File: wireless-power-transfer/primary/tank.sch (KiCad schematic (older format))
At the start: 6 parts

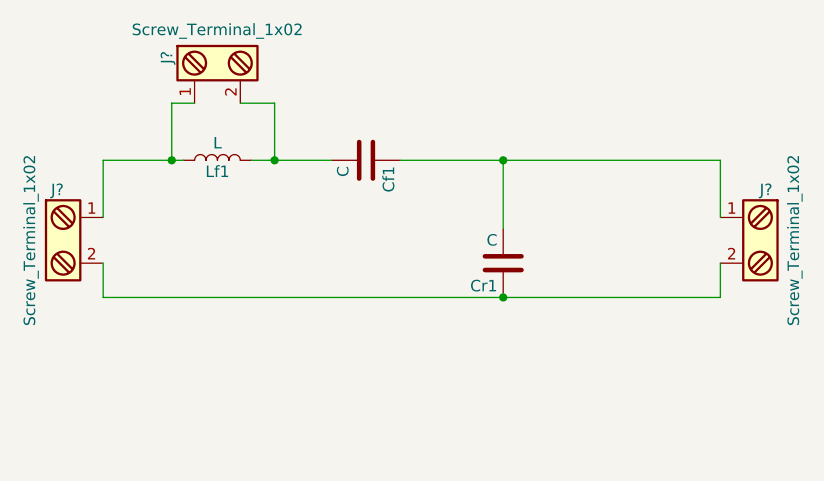
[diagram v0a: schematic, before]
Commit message: Added pcb with tank and filter of the primary, some logos and other minor changes.
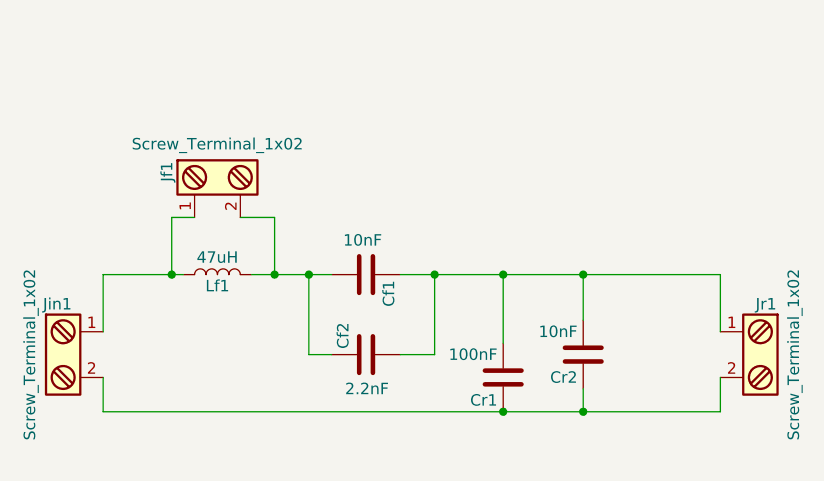
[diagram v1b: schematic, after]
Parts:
- added Cf2: 2.2nF, Capacitors_THT:C_Rect_L18.0mm_W5.0mm_P15.00mm_FKS3_FKP3, symbol C
- added Cr2: 10nF, Capacitors_THT:C_Rect_L18.0mm_W6.0mm_P15.00mm_FKS3_FKP3, symbol C
- Cf1: value C -> 10nF; footprint (none) -> Capacitors_THT:C_Rect_L18.0mm_W6.0mm_P15.00mm_FKS3_FKP3
- Cr1: value C -> 100nF; footprint (none) -> Capacitors_THT:C_Rect_L18.0mm_W5.0mm_P15.00mm_FKS3_FKP3
- Jf1, Jin1, Jr1: renamed from J?; footprint (none) -> Connectors_Terminal_Blocks:TerminalBlock_Pheonix_MKDS1.5-2pol
- Lf1: value L -> 47uH; footprint (none) -> componentesGIT:MuRata 1500 47u
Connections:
- net at Cr1.1, Jin1.2, Jr1.2: now also Cr2.1
- net at Cf1.2, Jf1.2, Lf1.2: now also Cf2.1
- net at Cf1.1, Cr1.2, Jr1.1: now also Cf2.2, Cr2.2
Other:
- moved on the sheet: Cf1, Cr1, Jf1, Jin1, Jr1, Lf1
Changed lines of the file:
@@
 $EndDescr
 $Comp
-L Screw_Terminal_1x02 J?
+L Screw_Terminal_1x02 Jin1
 U 1 1 59F1ACFF
-P 4500 3150
-F 0 "J?" H 4500 3400 50  0000 C TNN
-F 1 "Screw_Terminal_1x02" V 4350 3150 50  0000 C TNN
-F 2 "" H 4500 2925 50  0001 C CNN
-F 3 "" H 4475 3150 50  0001 C CNN
-	1    4500 3150
+P 4500 3650
+F 0 "Jin1" H 4500 3900 50  0000 C TNN
+F 1 "Screw_Terminal_1x02" V 4350 3650 50  0000 C TNN
+F 2 "Connectors_Terminal_Blocks:TerminalBlock_Pheonix_MKDS1.5-2pol" H 4500 3425 50  0001 C CNN
+F 3 "" H 4475 3650 50  0001 C CNN
+	1    4500 3650
 	1    0    0    -1
 $EndComp
@@
 L L Lf1
 U 1 1 59F1AF47
-P 5200 2800
-F 0 "Lf1" V 5150 2800 50  0000 C CNN
-F 1 "L" V 5275 2800 50  0000 C CNN
-F 2 "" H 5200 2800 50  0001 C CNN
-F 3 "" H 5200 2800 50  0001 C CNN
-	1    5200 2800
+P 5200 3300
+F 0 "Lf1" V 5150 3300 50  0000 C CNN
+F 1 "47uH" V 5275 3300 50  0000 C CNN
+F 2 "componentesGIT:MuRata 1500 47u" H 5200 3300 50  0001 C CNN
+F 3 "" H 5200 3300 50  0001 C CNN
+	1    5200 3300
 	0    -1   -1   0
 $EndComp
@@
 L C Cf1
 U 1 1 59F1B01C
-P 5850 2800
-F 0 "Cf1" H 5875 2900 50  0000 L CNN
-F 1 "C" H 5875 2700 50  0000 L CNN
-F 2 "" H 5888 2650 50  0001 C CNN
-F 3 "" H 5850 2800 50  0001 C CNN
-	1    5850 2800
+P 5850 3300
+F 0 "Cf1" H 5875 3400 50  0000 L CNN
+F 1 "10nF" V 5700 3200 50  0000 L CNN
+F 2 "Capacitors_THT:C_Rect_L18.0mm_W6.0mm_P15.00mm_FKS3_FKP3" H 5888 3150 50  0001 C CNN
+F 3 "" H 5850 3300 50  0001 C CNN
+	1    5850 3300
 	0    1    1    0
 $EndComp
@@
 L C Cr1
 U 1 1 59F1B0F0
-P 6450 3250
-F 0 "Cr1" H 6475 3350 50  0000 L CNN
-F 1 "C" H 6475 3150 50  0000 L CNN
-F 2 "" H 6488 3100 50  0001 C CNN
-F 3 "" H 6450 3250 50  0001 C CNN
-	1    6450 3250
+P 6450 3750
+F 0 "Cr1" H 6475 3850 50  0000 L CNN
+F 1 "100nF" H 6475 3650 50  0000 L CNN
+F 2 "Capacitors_THT:C_Rect_L18.0mm_W5.0mm_P15.00mm_FKS3_FKP3" H 6488 3600 50  0001 C CNN
+F 3 "" H 6450 3750 50  0001 C CNN
+	1    6450 3750
 	-1   0    0    1
 $EndComp
 $Comp
-L Screw_Terminal_1x02 J?
+L Screw_Terminal_1x02 Jr1
 U 1 1 59F1B13E
-P 7600 3150
-F 0 "J?" H 7600 3400 50  0000 C TNN
-F 1 "Screw_Terminal_1x02" V 7450 3150 50  0000 C TNN
-F 2 "" H 7600 2925 50  0001 C CNN
-F 3 "" H 7575 3150 50  0001 C CNN
-	1    7600 3150
+P 7600 3650
+F 0 "Jr1" H 7600 3900 50  0000 C TNN
+F 1 "Screw_Terminal_1x02" V 7450 3650 50  0000 C TNN
+F 2 "Connectors_Terminal_Blocks:TerminalBlock_Pheonix_MKDS1.5-2pol" H 7600 3425 50  0001 C CNN
+F 3 "" H 7575 3650 50  0001 C CNN
+	1    7600 3650
 	-1   0    0    -1
 $EndComp
 Wire Wire Line
-	4700 3050 4700 2800
+	4700 3550 4700 3300
 Wire Wire Line
-	4700 2800 5050 2800
+	4700 3300 5050 3300
 Wire Wire Line
-	5350 2800 5700 2800
+	5350 3300 5700 3300
 Wire Wire Line
-	6000 2800 7400 2800
+	6000 3300 7400 3300
 Wire Wire Line
-	6450 2800 6450 3100
+	6450 3300 6450 3600
 Wire Wire Line
-	7400 2800 7400 3050
+	7400 3300 7400 3550
 Wire Wire Line
-	7400 3400 7400 3250
+	7400 3900 7400 3750
 Wire Wire Line
-	4700 3400 7400 3400
-Connection ~ 6450 2800
+	4700 3900 7400 3900
+Connection ~ 6450 3300
 Wire Wire Line
-	4700 3400 4700 3250
-Connection ~ 6450 3400
+	4700 3900 4700 3750
+Connection ~ 6450 3900
 $Comp
-L Screw_Terminal_1x02 J?
+L Screw_Terminal_1x02 Jf1
 U 1 1 59F1B5CA
-P 5200 2350
-F 0 "J?" H 5200 2600 50  0000 C TNN
-F 1 "Screw_Terminal_1x02" V 5050 2350 50  0000 C TNN
-F 2 "" H 5200 2125 50  0001 C CNN
-F 3 "" H 5175 2350 50  0001 C CNN
-	1    5200 2350
+P 5200 2850
+F 0 "Jf1" H 5200 3100 50  0000 C TNN
+F 1 "Screw_Terminal_1x02" V 5050 2850 50  0000 C TNN
+F 2 "Connectors_Terminal_Blocks:TerminalBlock_Pheonix_MKDS1.5-2pol" H 5200 2625 50  0001 C CNN
+F 3 "" H 5175 2850 50  0001 C CNN
+	1    5200 2850
 	0    -1   1    0
 $EndComp
 Wire Wire Line
-	5000 2800 5000 2550
+	5000 3300 5000 3050
 Wire Wire Line
-	5000 2550 5100 2550
-Connection ~ 5000 2800
+	5000 3050 5100 3050
+Connection ~ 5000 3300
 Wire Wire Line
-	5450 2800 5450 2550
+	5450 3300 5450 3050
 Wire Wire Line
-	5450 2550 5300 2550
-Connection ~ 5450 2800
+	5450 3050 5300 3050
+Connection ~ 5450 3300
+$Comp
+L C Cr2
+U 1 1 59F1A45D
+P 6800 3650
+F 0 "Cr2" H 6825 3750 50  0000 L CNN
+F 1 "10nF" H 6825 3550 50  0000 L CNN
+F 2 "Capacitors_THT:C_Rect_L18.0mm_W6.0mm_P15.00mm_FKS3_FKP3" H 6838 3500 50  0001 C CNN
+F 3 "" H 6800 3650 50  0001 C CNN
+	1    6800 3650
+	-1   0    0    1
+$EndComp
+$Comp
+L C Cf2
+U 1 1 59F1A4A3
+P 5850 3650
+F 0 "Cf2" H 5875 3750 50  0000 L CNN
+F 1 "2.2nF" V 5700 3550 50  0000 L CNN
+F 2 "Capacitors_THT:C_Rect_L18.0mm_W5.0mm_P15.00mm_FKS3_FKP3" H 5888 3500 50  0001 C CNN
+F 3 "" H 5850 3650 50  0001 C CNN
+	1    5850 3650
+	0    -1   -1   0
+$EndComp
+Wire Wire Line
+	6800 3500 6800 3300
+Connection ~ 6800 3300
+Wire Wire Line
+	6800 3800 6800 3900
+Connection ~ 6800 3900
+Wire Wire Line
+	6000 3650 6150 3650
+Wire Wire Line
+	6150 3650 6150 3300
+Connection ~ 6150 3300
+Wire Wire Line
+	5700 3650 5600 3650
+Wire Wire Line
+	5600 3650 5600 3300
+Connection ~ 5600 3300
 $EndSCHEMATC

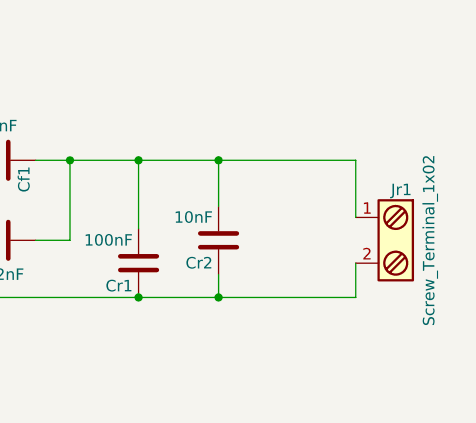
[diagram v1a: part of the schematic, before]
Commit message: Added a second connector for resonant coil of the primary.
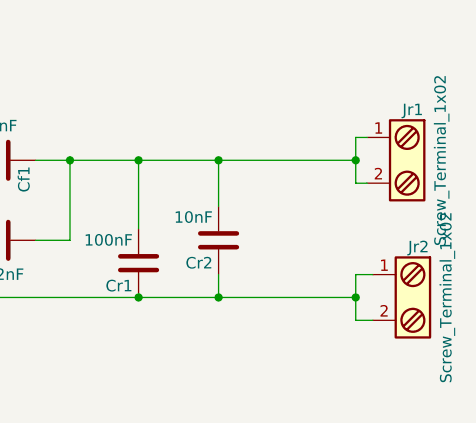
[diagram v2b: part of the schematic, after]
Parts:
- added Jr2: Screw_Terminal_1x02, Connectors_Terminal_Blocks:TerminalBlock_Pheonix_MKDS1.5-2pol, symbol Screw_Terminal_1x02
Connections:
- net at Cr1.1, Cr2.1, Jin1.2: now also Jr2.1, Jr2.2; no longer Jr1.2
- net at Cf1.1, Cf2.2, Cr1.2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: now also Jr1.2
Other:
- moved on the sheet: Jr1
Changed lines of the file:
@@
 L Screw_Terminal_1x02 Jr1
 U 1 1 59F1B13E
-P 7600 3650
-F 0 "Jr1" H 7600 3900 50  0000 C TNN
-F 1 "Screw_Terminal_1x02" V 7450 3650 50  0000 C TNN
-F 2 "Connectors_Terminal_Blocks:TerminalBlock_Pheonix_MKDS1.5-2pol" H 7600 3425 50  0001 C CNN
-F 3 "" H 7575 3650 50  0001 C CNN
-	1    7600 3650
+P 7650 3300
+F 0 "Jr1" H 7650 3550 50  0000 C TNN
+F 1 "Screw_Terminal_1x02" V 7500 3300 50  0000 C TNN
+F 2 "Connectors_Terminal_Blocks:TerminalBlock_Pheonix_MKDS1.5-2pol" H 7650 3075 50  0001 C CNN
+F 3 "" H 7625 3300 50  0001 C CNN
+	1    7650 3300
 	-1   0    0    -1
 $EndComp
@@
 Wire Wire Line
 	6450 3300 6450 3600
-Wire Wire Line
-	7400 3300 7400 3550
-Wire Wire Line
-	7400 3900 7400 3750
 Wire Wire Line
 	4700 3900 7400 3900
@@
 	5600 3650 5600 3300
 Connection ~ 5600 3300
+Wire Wire Line
+	7400 3200 7400 3400
+Wire Wire Line
+	7400 3200 7450 3200
+Wire Wire Line
+	7400 3400 7450 3400
+Connection ~ 7400 3300
+$Comp
+L Screw_Terminal_1x02 Jr2
+U 1 1 59F74076
+P 7675 3900
+F 0 "Jr2" H 7675 4150 50  0000 C TNN
+F 1 "Screw_Terminal_1x02" V 7525 3900 50  0000 C TNN
+F 2 "Connectors_Terminal_Blocks:TerminalBlock_Pheonix_MKDS1.5-2pol" H 7675 3675 50  0001 C CNN
+F 3 "" H 7650 3900 50  0001 C CNN
+	1    7675 3900
+	-1   0    0    -1
+$EndComp
+Wire Wire Line
+	7400 3800 7400 4000
+Wire Wire Line
+	7400 3800 7475 3800
+Wire Wire Line
+	7400 4000 7475 4000
+Connection ~ 7400 3900
 $EndSCHEMATC

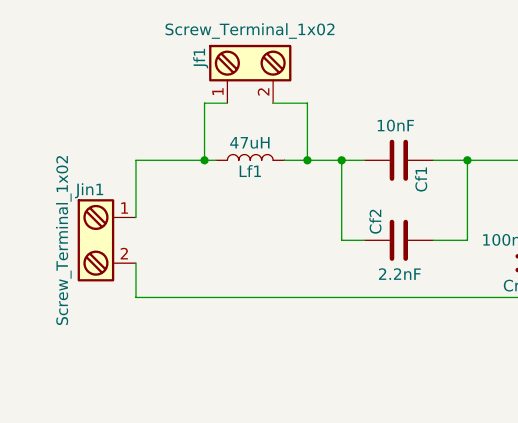
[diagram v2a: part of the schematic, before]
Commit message: The two PCBs of the primary circuit have been connected.
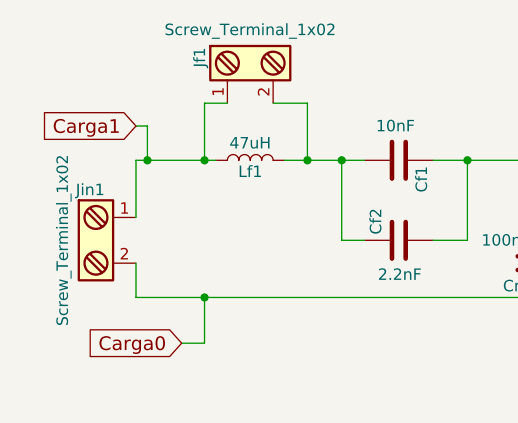
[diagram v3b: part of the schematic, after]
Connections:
- net Carga0: now reaches Cr1.1, Cr2.1, Jin1.2, Jr2.1, Jr2.2
- net Carga1: now reaches Jf1.1, Jin1.1, Lf1.1
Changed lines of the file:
@@
 LIBS:r-78exx
 LIBS:switches
-LIBS:xbee_wi-fi
 LIBS:irlb8721pbf
 LIBS:tfg-cache
@@
 	7400 4000 7475 4000
 Connection ~ 7400 3900
+Text GLabel 4700 3150 0    60   Input ~ 0
+Carga1
+Text GLabel 4900 4100 0    60   Input ~ 0
+Carga0
+Wire Wire Line
+	4700 3150 4750 3150
+Wire Wire Line
+	4750 3150 4750 3300
+Connection ~ 4750 3300
+Wire Wire Line
+	4900 4100 5000 4100
+Wire Wire Line
+	5000 4100 5000 3900
+Connection ~ 5000 3900
 $EndSCHEMATC

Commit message: PDFs created with schematics and PCB layers for front and back sides.
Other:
- note added: "2/7"
- moved on the sheet: Cf1, Cf2, Cr1, Cr2, Jf1, Jin1, Jr1, Jr2, Lf1
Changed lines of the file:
@@
 EESchema Schematic File Version 2
+LIBS:tfg-rescue
 LIBS:power
 LIBS:device
@@
 LIBS:r-78exx
 LIBS:switches
+LIBS:xbee_wi-fi
 LIBS:irlb8721pbf
 LIBS:tfg-cache
 EELAYER 25 0
 EELAYER END
-$Descr A4 11693 8268
+$Descr A4 8268 11693 portrait
 encoding utf-8
 Sheet 2 2
@@
 L Screw_Terminal_1x02 Jin1
 U 1 1 59F1ACFF
-P 4500 3650
-F 0 "Jin1" H 4500 3900 50  0000 C TNN
-F 1 "Screw_Terminal_1x02" V 4350 3650 50  0000 C TNN
-F 2 "Connectors_Terminal_Blocks:TerminalBlock_Pheonix_MKDS1.5-2pol" H 4500 3425 50  0001 C CNN
-F 3 "" H 4475 3650 50  0001 C CNN
-	1    4500 3650
+P 2800 4500
+F 0 "Jin1" H 2800 4750 50  0000 C TNN
+F 1 "Screw_Terminal_1x02" V 2650 4500 50  0000 C TNN
+F 2 "Connectors_Terminal_Blocks:TerminalBlock_Pheonix_MKDS1.5-2pol" H 2800 4275 50  0001 C CNN
+F 3 "" H 2775 4500 50  0001 C CNN
+	1    2800 4500
 	1    0    0    -1
 $EndComp
@@
 L L Lf1
 U 1 1 59F1AF47
-P 5200 3300
-F 0 "Lf1" V 5150 3300 50  0000 C CNN
-F 1 "47uH" V 5275 3300 50  0000 C CNN
-F 2 "componentesGIT:MuRata 1500 47u" H 5200 3300 50  0001 C CNN
-F 3 "" H 5200 3300 50  0001 C CNN
-	1    5200 3300
+P 3500 4150
+F 0 "Lf1" V 3450 4150 50  0000 C CNN
+F 1 "47uH" V 3575 4150 50  0000 C CNN
+F 2 "componentesGIT:MuRata 1500 47u" H 3500 4150 50  0001 C CNN
+F 3 "" H 3500 4150 50  0001 C CNN
+	1    3500 4150
 	0    -1   -1   0
 $EndComp
@@
 L C Cf1
 U 1 1 59F1B01C
-P 5850 3300
-F 0 "Cf1" H 5875 3400 50  0000 L CNN
-F 1 "10nF" V 5700 3200 50  0000 L CNN
-F 2 "Capacitors_THT:C_Rect_L18.0mm_W6.0mm_P15.00mm_FKS3_FKP3" H 5888 3150 50  0001 C CNN
-F 3 "" H 5850 3300 50  0001 C CNN
-	1    5850 3300
+P 4150 4150
+F 0 "Cf1" V 4225 4200 50  0000 L CNN
+F 1 "10nF" V 4000 4050 50  0000 L CNN
+F 2 "Capacitors_THT:C_Rect_L18.0mm_W6.0mm_P15.00mm_FKS3_FKP3" H 4188 4000 50  0001 C CNN
+F 3 "" H 4150 4150 50  0001 C CNN
+	1    4150 4150
 	0    1    1    0
 $EndComp
@@
 L C Cr1
 U 1 1 59F1B0F0
-P 6450 3750
-F 0 "Cr1" H 6475 3850 50  0000 L CNN
-F 1 "100nF" H 6475 3650 50  0000 L CNN
-F 2 "Capacitors_THT:C_Rect_L18.0mm_W5.0mm_P15.00mm_FKS3_FKP3" H 6488 3600 50  0001 C CNN
-F 3 "" H 6450 3750 50  0001 C CNN
-	1    6450 3750
+P 4750 4450
+F 0 "Cr1" H 4775 4550 50  0000 L CNN
+F 1 "100nF" H 4775 4350 50  0000 L CNN
+F 2 "Capacitors_THT:C_Rect_L18.0mm_W5.0mm_P15.00mm_FKS3_FKP3" H 4788 4300 50  0001 C CNN
+F 3 "" H 4750 4450 50  0001 C CNN
+	1    4750 4450
 	-1   0    0    1
 $EndComp
@@
 L Screw_Terminal_1x02 Jr1
 U 1 1 59F1B13E
-P 7650 3300
-F 0 "Jr1" H 7650 3550 50  0000 C TNN
-F 1 "Screw_Terminal_1x02" V 7500 3300 50  0000 C TNN
-F 2 "Connectors_Terminal_Blocks:TerminalBlock_Pheonix_MKDS1.5-2pol" H 7650 3075 50  0001 C CNN
-F 3 "" H 7625 3300 50  0001 C CNN
-	1    7650 3300
+P 5950 4150
+F 0 "Jr1" H 5950 4400 50  0000 C TNN
+F 1 "Screw_Terminal_1x02" V 5800 4150 50  0000 C TNN
+F 2 "Connectors_Terminal_Blocks:TerminalBlock_Pheonix_MKDS1.5-2pol" H 5950 3925 50  0001 C CNN
+F 3 "" H 5925 4150 50  0001 C CNN
+	1    5950 4150
 	-1   0    0    -1
 $EndComp
 Wire Wire Line
-	4700 3550 4700 3300
-Wire Wire Line
-	4700 3300 5050 3300
-Wire Wire Line
-	5350 3300 5700 3300
-Wire Wire Line
-	6000 3300 7400 3300
-Wire Wire Line
-	6450 3300 6450 3600
-Wire Wire Line
-	4700 3900 7400 3900
-Connection ~ 6450 3300
-Wire Wire Line
-	4700 3900 4700 3750
-Connection ~ 6450 3900
+	3000 4400 3000 4150
+Wire Wire Line
+	3000 4150 3350 4150
+Wire Wire Line
+	3650 4150 4000 4150
+Wire Wire Line
+	4300 4150 5700 4150
+Wire Wire Line
+	3000 4750 5700 4750
+Connection ~ 4750 4150
+Wire Wire Line
+	3000 4750 3000 4600
+Connection ~ 4750 4750
 $Comp
 L Screw_Terminal_1x02 Jf1
 U 1 1 59F1B5CA
-P 5200 2850
-F 0 "Jf1" H 5200 3100 50  0000 C TNN
-F 1 "Screw_Terminal_1x02" V 5050 2850 50  0000 C TNN
-F 2 "Connectors_Terminal_Blocks:TerminalBlock_Pheonix_MKDS1.5-2pol" H 5200 2625 50  0001 C CNN
-F 3 "" H 5175 2850 50  0001 C CNN
-	1    5200 2850
+P 3500 3700
+F 0 "Jf1" H 3500 3950 50  0000 C TNN
+F 1 "Screw_Terminal_1x02" V 3350 3700 50  0000 C TNN
+F 2 "Connectors_Terminal_Blocks:TerminalBlock_Pheonix_MKDS1.5-2pol" H 3500 3475 50  0001 C CNN
+F 3 "" H 3475 3700 50  0001 C CNN
+	1    3500 3700
 	0    -1   1    0
 $EndComp
 Wire Wire Line
-	5000 3300 5000 3050
-Wire Wire Line
-	5000 3050 5100 3050
-Connection ~ 5000 3300
-Wire Wire Line
-	5450 3300 5450 3050
-Wire Wire Line
-	5450 3050 5300 3050
-Connection ~ 5450 3300
+	3300 4150 3300 3900
+Wire Wire Line
+	3300 3900 3400 3900
+Connection ~ 3300 4150
+Wire Wire Line
+	3750 4150 3750 3900
+Wire Wire Line
+	3750 3900 3600 3900
+Connection ~ 3750 4150
 $Comp
 L C Cr2
 U 1 1 59F1A45D
-P 6800 3650
-F 0 "Cr2" H 6825 3750 50  0000 L CNN
-F 1 "10nF" H 6825 3550 50  0000 L CNN
-F 2 "Capacitors_THT:C_Rect_L18.0mm_W6.0mm_P15.00mm_FKS3_FKP3" H 6838 3500 50  0001 C CNN
-F 3 "" H 6800 3650 50  0001 C CNN
-	1    6800 3650
+P 5100 4450
+F 0 "Cr2" H 5125 4550 50  0000 L CNN
+F 1 "10nF" H 5125 4350 50  0000 L CNN
+F 2 "Capacitors_THT:C_Rect_L18.0mm_W6.0mm_P15.00mm_FKS3_FKP3" H 5138 4300 50  0001 C CNN
+F 3 "" H 5100 4450 50  0001 C CNN
+	1    5100 4450
 	-1   0    0    1
 $EndComp
@@
 L C Cf2
 U 1 1 59F1A4A3
-P 5850 3650
-F 0 "Cf2" H 5875 3750 50  0000 L CNN
-F 1 "2.2nF" V 5700 3550 50  0000 L CNN
-F 2 "Capacitors_THT:C_Rect_L18.0mm_W5.0mm_P15.00mm_FKS3_FKP3" H 5888 3500 50  0001 C CNN
-F 3 "" H 5850 3650 50  0001 C CNN
-	1    5850 3650
+P 4150 4500
+F 0 "Cf2" V 4225 4325 50  0000 L CNN
+F 1 "2.2nF" V 4000 4400 50  0000 L CNN
+F 2 "Capacitors_THT:C_Rect_L18.0mm_W5.0mm_P15.00mm_FKS3_FKP3" H 4188 4350 50  0001 C CNN
+F 3 "" H 4150 4500 50  0001 C CNN
+	1    4150 4500
 	0    -1   -1   0
 $EndComp
-Wire Wire Line
-	6800 3500 6800 3300
-Connection ~ 6800 3300
-Wire Wire Line
-	6800 3800 6800 3900
-Connection ~ 6800 3900
-Wire Wire Line
-	6000 3650 6150 3650
-Wire Wire Line
-	6150 3650 6150 3300
-Connection ~ 6150 3300
-Wire Wire Line
-	5700 3650 5600 3650
-Wire Wire Line
-	5600 3650 5600 3300
-Connection ~ 5600 3300
-Wire Wire Line
-	7400 3200 7400 3400
-Wire Wire Line
-	7400 3200 7450 3200
-Wire Wire Line
-	7400 3400 7450 3400
-Connection ~ 7400 3300
+Connection ~ 5100 4150
+Wire Wire Line
+	5100 4600 5100 4750
+Connection ~ 5100 4750
+Wire Wire Line
+	4300 4500 4450 4500
+Wire Wire Line
+	4450 4500 4450 4150
+Connection ~ 4450 4150
+Wire Wire Line
+	4000 4500 3900 4500
+Wire Wire Line
+	3900 4500 3900 4150
+Connection ~ 3900 4150
+Wire Wire Line
+	5700 4050 5700 4250
+Wire Wire Line
+	5700 4050 5750 4050
+Wire Wire Line
+	5700 4250 5750 4250
+Connection ~ 5700 4150
 $Comp
 L Screw_Terminal_1x02 Jr2
 U 1 1 59F74076
-P 7675 3900
-F 0 "Jr2" H 7675 4150 50  0000 C TNN
-F 1 "Screw_Terminal_1x02" V 7525 3900 50  0000 C TNN
-F 2 "Connectors_Terminal_Blocks:TerminalBlock_Pheonix_MKDS1.5-2pol" H 7675 3675 50  0001 C CNN
-F 3 "" H 7650 3900 50  0001 C CNN
-	1    7675 3900
+P 5975 4750
+F 0 "Jr2" H 5975 5000 50  0000 C TNN
+F 1 "Screw_Terminal_1x02" V 5825 4750 50  0000 C TNN
+F 2 "Connectors_Terminal_Blocks:TerminalBlock_Pheonix_MKDS1.5-2pol" H 5975 4525 50  0001 C CNN
+F 3 "" H 5950 4750 50  0001 C CNN
+	1    5975 4750
 	-1   0    0    -1
 $EndComp
 Wire Wire Line
-	7400 3800 7400 4000
-Wire Wire Line
-	7400 3800 7475 3800
-Wire Wire Line
-	7400 4000 7475 4000
-Connection ~ 7400 3900
-Text GLabel 4700 3150 0    60   Input ~ 0
+	5700 4650 5700 4850
+Wire Wire Line
+	5700 4650 5775 4650
+Wire Wire Line
+	5700 4850 5775 4850
+Connection ~ 5700 4750
+Text GLabel 3000 4000 0    60   Input ~ 0
 Carga1
-Text GLabel 4900 4100 0    60   Input ~ 0
+Text GLabel 3200 4950 0    60   Input ~ 0
 Carga0
 Wire Wire Line
-	4700 3150 4750 3150
-Wire Wire Line
-	4750 3150 4750 3300
-Connection ~ 4750 3300
-Wire Wire Line
-	4900 4100 5000 4100
-Wire Wire Line
-	5000 4100 5000 3900
-Connection ~ 5000 3900
+	3000 4000 3050 4000
+Wire Wire Line
+	3050 4000 3050 4150
+Connection ~ 3050 4150
+Wire Wire Line
+	3200 4950 3300 4950
+Wire Wire Line
+	3300 4950 3300 4750
+Connection ~ 3300 4750
+Wire Wire Line
+	4750 4150 4750 4300
+Wire Wire Line
+	4750 4600 4750 4750
+Wire Wire Line
+	5100 4300 5100 4150
+Text Notes 6850 11025 0    118  ~ 0
+2/7
 $EndSCHEMATC
